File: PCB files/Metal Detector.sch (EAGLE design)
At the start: 105 parts, among them IC1 NE5534AD, IC2 BQ24133RGYR, IC4 ESP32-WROOM-32UE-N4, IC6 TLV62130ARGTR, IC7 TLV1117-33IDCYR, J1 DG128-7.5, J2 DG128-7.5, Q1 IRF740, Q11 MMBT3904, Q3 SI2312CDS-T1-GE3, Q5 SI2312CDS-T1-GE3, Q6 SI2323CDS-T1-GE3, Q9 MMBT3904, X2 DC21MMX

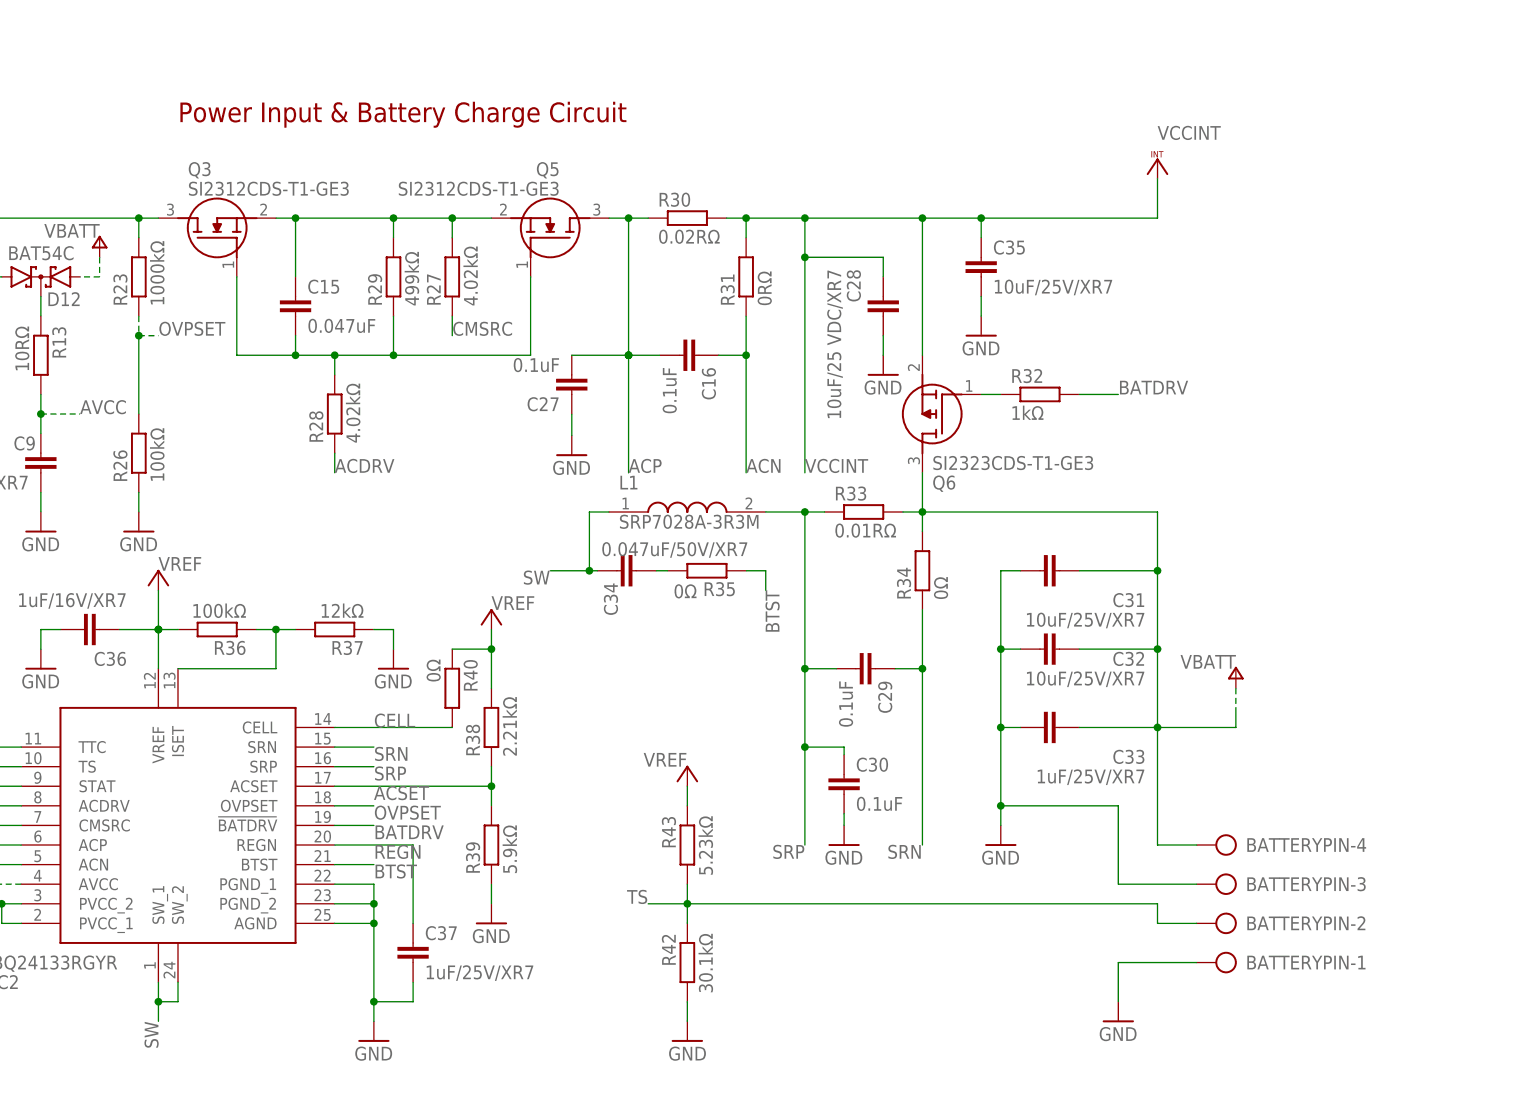
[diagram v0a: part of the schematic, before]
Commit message: Add files via upload
Started design PCB layout first start from battery charge circut, still desing process
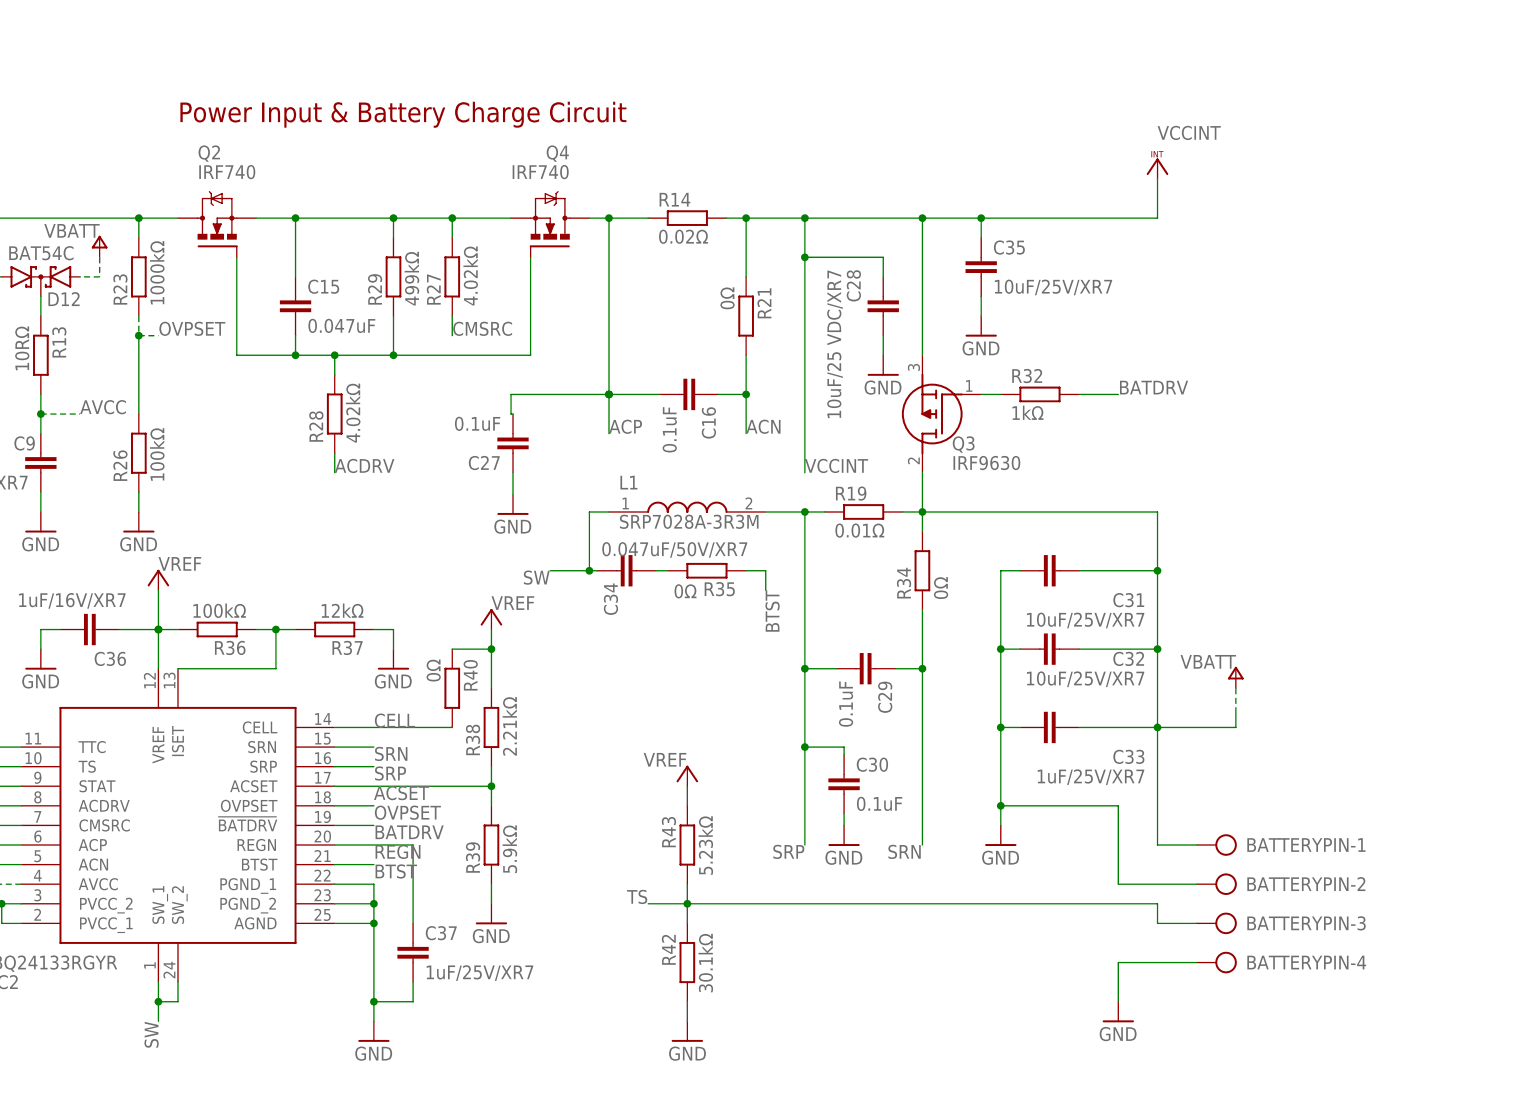
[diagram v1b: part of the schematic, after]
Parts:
- removed Q5: SI2312CDS-T1-GE3, SI2312CDS-T1-GE3:SI2312CDS-T1-GE3
- removed Q6: SI2323CDS-T1-GE3, SI2323CDS-T1-GE3:SI2323CDS-T1-GE3
- removed R30: 0.02RΩ, rcl:R-EU_R1206
- removed R31: 0RΩ, rcl:R-EU_R1206
- removed R33: 0.01RΩ, rcl:R-EU_R1206
- added Q2, Q4: IRF740, IRF740:IRF740
- added R14: 0.02Ω, rcl:R-EU_R2010
- added R19: 0.01Ω, rcl:R-EU_R2010
- added R21: 0Ω, rcl:R-EU_R0603
- Q3: value SI2312CDS-T1-GE3 -> IRF9630; device SI2312CDS-T1-GE3:SI2312CDS-T1-GE3 -> IRF9630:IRF9630
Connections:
- net 12V_IN: now also Q2.D; no longer Q3.D
- net ACN: now also R21.2; no longer R31.1
- net ACP: now also Q4.D, R14.1; no longer Q5.D, R30.1
- net GND: now also BATTERYPIN-2.KL, BATTERYPIN-4.KL; no longer BATTERYPIN-1.KL, BATTERYPIN-3.KL
- net N$21: now also Q2.S, Q4.S; no longer Q3.S, Q5.S
- net N$22: now also Q2.G, Q4.G; no longer Q3.G, Q5.G
- net N$23: now also Q3.G; no longer Q6.G
- net SRP: now also R19.1; no longer R33.1
- net TS: now also BATTERYPIN-3.KL; no longer BATTERYPIN-2.KL
- net VBATT: now also BATTERYPIN-1.KL, Q3.D, R19.2; no longer BATTERYPIN-4.KL, Q6.D, R33.2
- net VCCINT: now also Q3.S, R14.2, R21.1; no longer Q6.S, R30.2, R31.2
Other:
- moved on the sheet: BATTERYPIN-1, BATTERYPIN-2, BATTERYPIN-3, BATTERYPIN-4, C16, C27, Q3
